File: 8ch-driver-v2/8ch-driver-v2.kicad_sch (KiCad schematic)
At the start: 36 parts, among them J1 Barrel_Jack, J2 Screw_Terminal_01x08, J3 Screw_Terminal_01x08, J4 Screw_Terminal_01x14, Q1 2N7002E, Q2 2N7002E, U1 DRV104PWP, U2 DRV104PWP

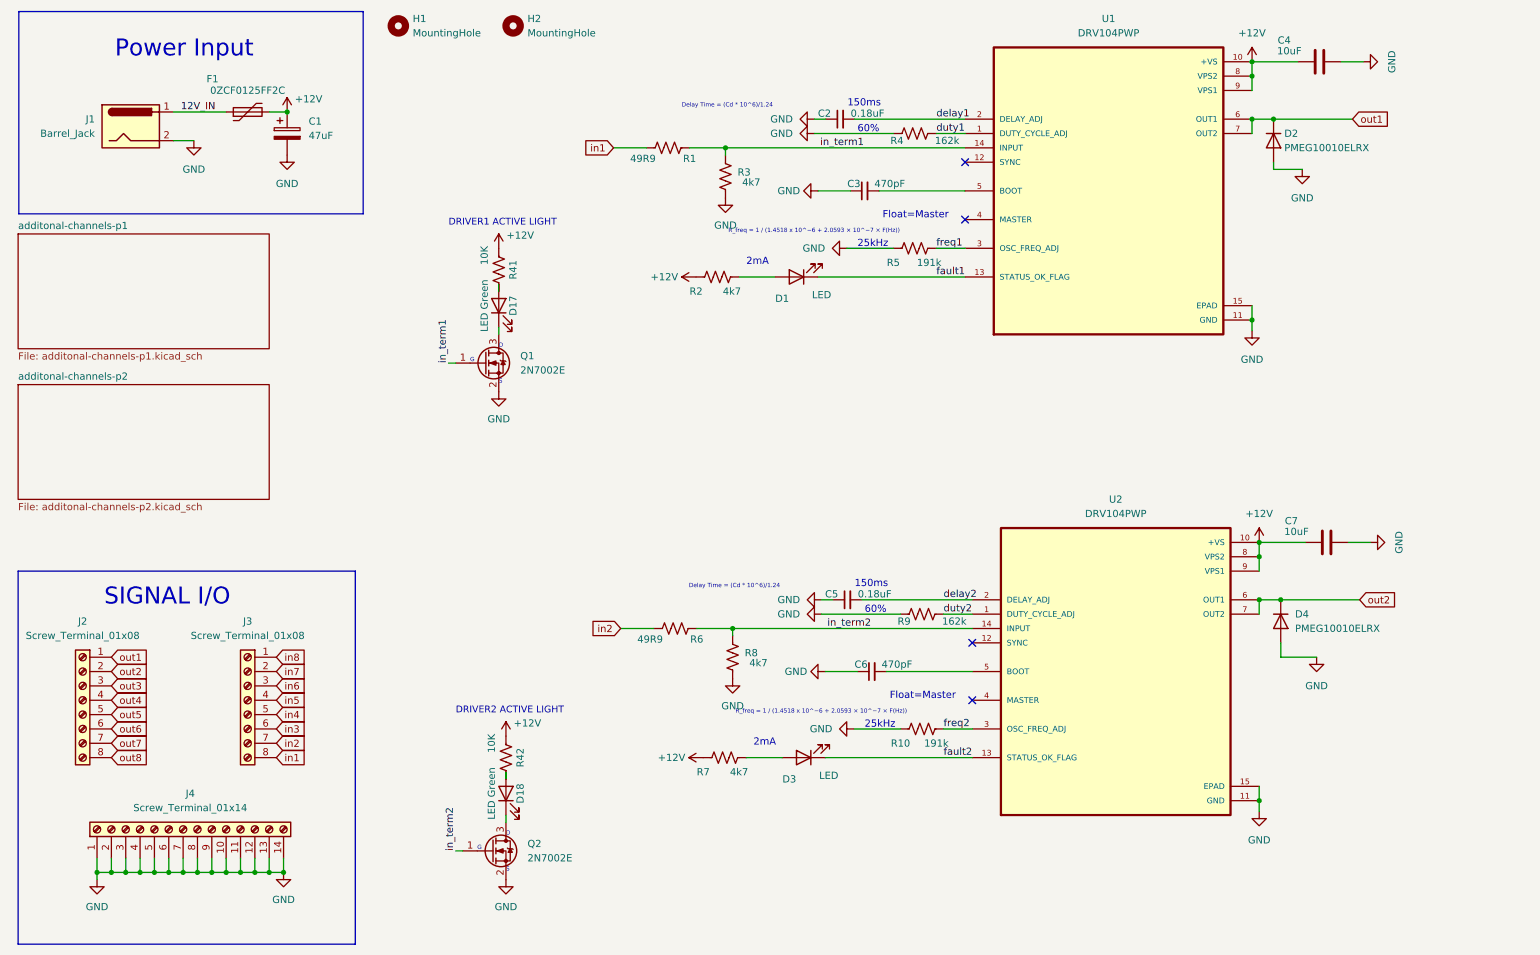
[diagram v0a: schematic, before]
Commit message: added 8 more channels and an FTDH chip
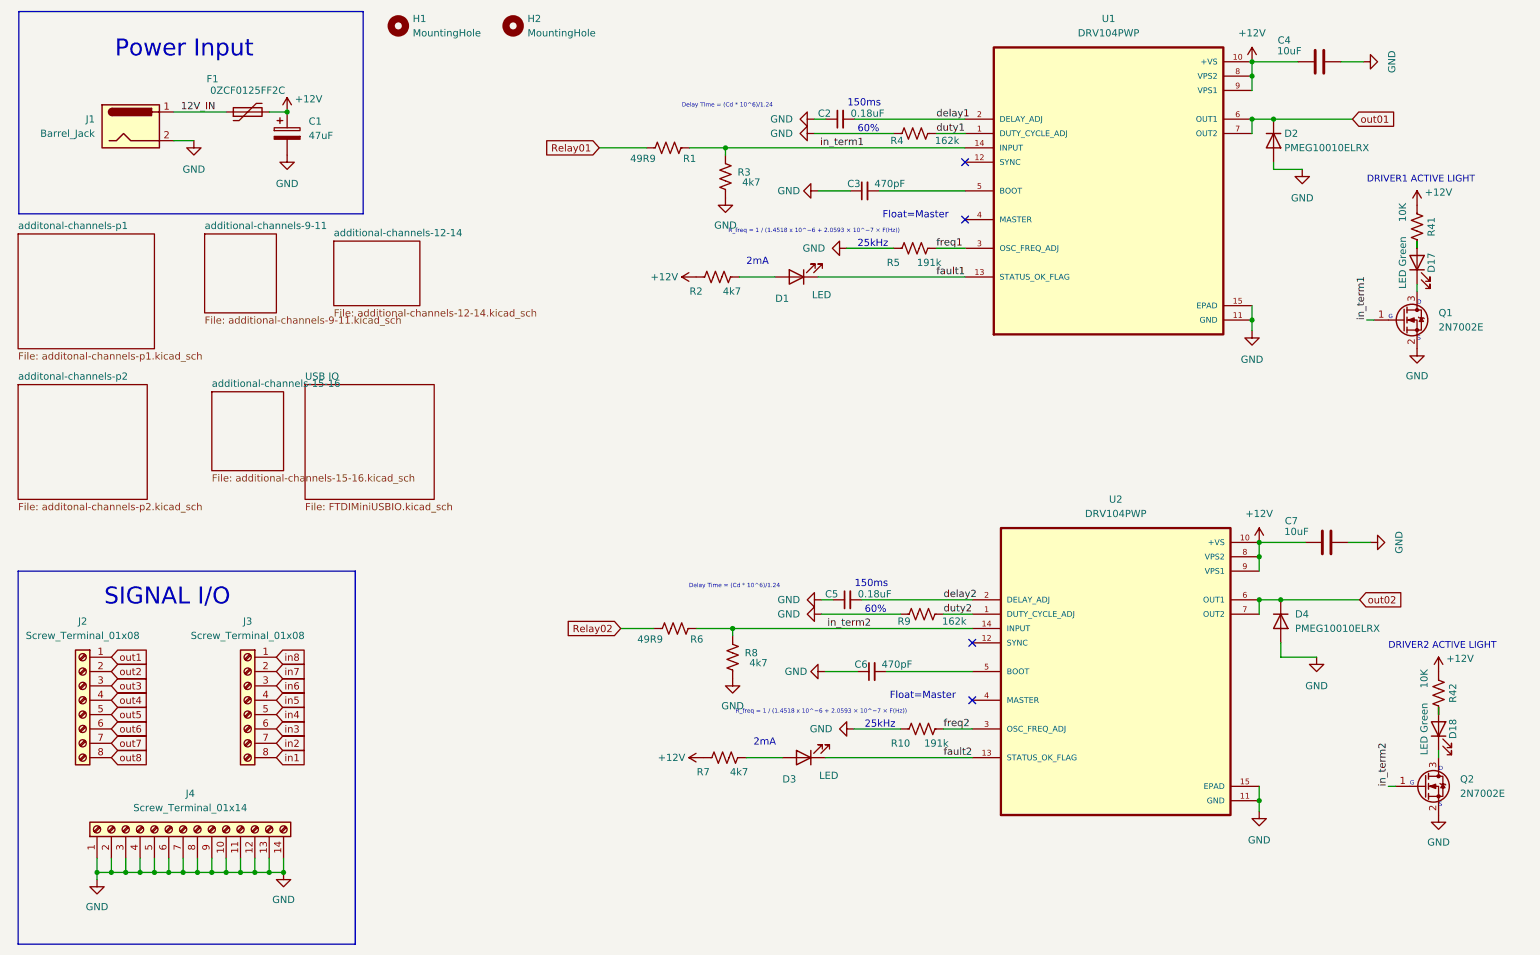
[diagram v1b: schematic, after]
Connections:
- net in1: no longer R1.1
- net in2: no longer R6.1
- net out1: no longer D2.1 (K), U1.6 (OUT1), U1.7 (OUT2)
- net out2: no longer D4.1 (K), U2.6 (OUT1), U2.7 (OUT2)
- new net Relay01: R1.1
- new net Relay02: R6.1
- new net out01: D2.1 (K), U1.6 (OUT1), U1.7 (OUT2)
- new net out02: D4.1 (K), U2.6 (OUT1), U2.7 (OUT2)
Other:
- added sheet USB IO (FTDIMiniUSBIO.kicad_sch)
- added sheet additional-channels-12-14 (additional-channels-12-14.kicad_sch)
- added sheet additional-channels-15-16 (additional-channels-15-16.kicad_sch)
- added sheet additional-channels-9-11 (additional-channels-9-11.kicad_sch)
- title: 8 Channel PWM Solenoid Driver -> 16 Channel PWM Solenoid Driver - USB
- moved on the sheet: D17, D18, Q1, Q2, R41, R42

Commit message: progress
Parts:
- removed J2, J3: Screw_Terminal_01x08, TerminalBlock_Phoenix:TerminalBlock_Phoenix_PT-1,5-8-5.0-H_1x08_P5.00mm_Horizontal, symbol Connector:Screw_Terminal_01x08
- removed J4: Screw_Terminal_01x14, TerminalBlock_Phoenix:TerminalBlock_Phoenix_PT-1,5-14-5.0-H_1x14_P5.00mm_Horizontal, symbol Connector:Screw_Terminal_01x14
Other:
- note removed: "SIGNAL I/O"

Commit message: mucho mas progresso
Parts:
- removed C2, C5: 0.18uF, Capacitor_SMD:C_1206_3216Metric, symbol Device:C_Small
- removed C4, C7: 10uF, Capacitor_SMD:C_1210_3225Metric, symbol Device:C
- removed D1: LED, LED_SMD:LED_0805_2012Metric, symbol Device:LED
- removed D17, D18: LED Green, LED_SMD:LED_0805_2012Metric, symbol Device:LED
- removed D2: PMEG10010ELRX, Diode_SMD:Nexperia_CFP3_SOD-123W, symbol Device:D
- removed R41, R42: 10K, Resistor_SMD:R_1206_3216Metric, symbol Device:R_US
- added C2, C5: 10uF, Capacitor_SMD:C_1210_3225Metric, symbol Device:C
- added C4, C7: 470pF, Capacitor_SMD:C_1206_3216Metric, symbol Device:C_Small
- added D1: PMEG10010ELRX, Diode_SMD:Nexperia_CFP3_SOD-123W, symbol Device:D
- added D2, D5: LED Green, LED_SMD:LED_0805_2012Metric, symbol Device:LED
- added D6: LED, LED_SMD:LED_0805_2012Metric, symbol Device:LED
- added R11: 191k, Resistor_SMD:R_1206_3216Metric, symbol Device:R_US
- added R12: 4k7, Resistor_SMD:R_1206_3216Metric, symbol Device:R_US
- C3, C6: value 470pF -> 0.18uF; Mfg Kemet -> KYOCERA AVX; PartNum C0805C471K5RAC7800 -> 08053C184KAT2A
- R1: value 49R9 -> 10K; PartNum RC0805FR-0749R9L -> RC0805FR-07162KL
- R10: value 191k -> 4k7; PartNum RC0805FR-07191KL -> RC0805JR-074K7L
- R2, R8: value 4k7 -> 162k; PartNum RC0805JR-074K7L -> RC0805FR-07162KL
- R3: value 4k7 -> 49R9; PartNum RC0805JR-074K7L -> RC0805FR-0749R9L
- R4: value 162k -> 4k7; PartNum RC0805FR-07162KL -> RC0805JR-074K7L
- R6: value 49R9 -> 4k7; PartNum RC0805FR-0749R9L -> RC0805JR-074K7L
- R7: value 4k7 -> 10K; PartNum RC0805JR-074K7L -> RC0805FR-07162KL
- R9: value 162k -> 49R9; PartNum RC0805FR-07162KL -> RC0805FR-0749R9L
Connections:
- net +12V: now also R1.1, R6.1, C2.1, C5.1, R12.1; no longer R2.1
- net GND: now also R2.1, C2.2, C4.1, C5.2, C7.1, D1.2 (A), R11.1; no longer R3.1, R9.1
- net Relay01: now also R3.1; no longer R1.1
- net Relay02: now also R9.1; no longer R6.1
- net out01: now also D1.1 (K)
- net at U1.5 (BOOT): now also C4.2; no longer C3.2
- net at R7.2: now also D5.2 (A); no longer D3.2 (A)
- net at U2.5 (BOOT): now also C7.2; no longer C6.2
- net at Q2.3 (D): now also D5.1 (K)
- net duty01: now reaches R2.2
- net duty01: now also U1.1 (DUTY_CYCLE_ADJ)
- net at Q1.3 (D): now also D2.1 (K)
- net delay1 renamed delay01
- net delay01: now also C3.2
- net delay2 renamed delay02
- net delay02: now also C6.2
- net duty1 renamed in_term01
- net in_term01: now also Q1.1 (G), R3.2, U1.14 (INPUT); no longer U1.1 (DUTY_CYCLE_ADJ)
- net duty2 renamed duty02
- net duty02: now also R8.2; no longer R9.2
- net fault1 renamed fault01
- net fault01: now also D3.1 (K)
- net fault2 renamed fault02
- net fault02: now also D6.1 (K); no longer D3.1 (K)
- net freq1 renamed freq01
- net freq2 renamed freq02
- net freq02: now also R11.2; no longer R10.2
- removed net in_term1: Q1.1 (G), R1.2, R3.2, U1.14 (INPUT)
- net in_term2 renamed in_term02
- net in_term02: now also R10.2, R9.2; no longer R6.2, R8.2
- new net: D3.2 (A), R6.2
- new net: D2.2 (A), R1.2
- new net: D6.2 (A), R12.2
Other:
- note added: "DRIVER6 ACTIVE LIGHT"
- note removed: "DRIVER1 ACTIVE LIGHT"
- note removed: "DRIVER2 ACTIVE LIGHT"
